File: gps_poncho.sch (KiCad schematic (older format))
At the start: 5 parts, among them J1 Micro_SD_Card, U11 SE868K3-A

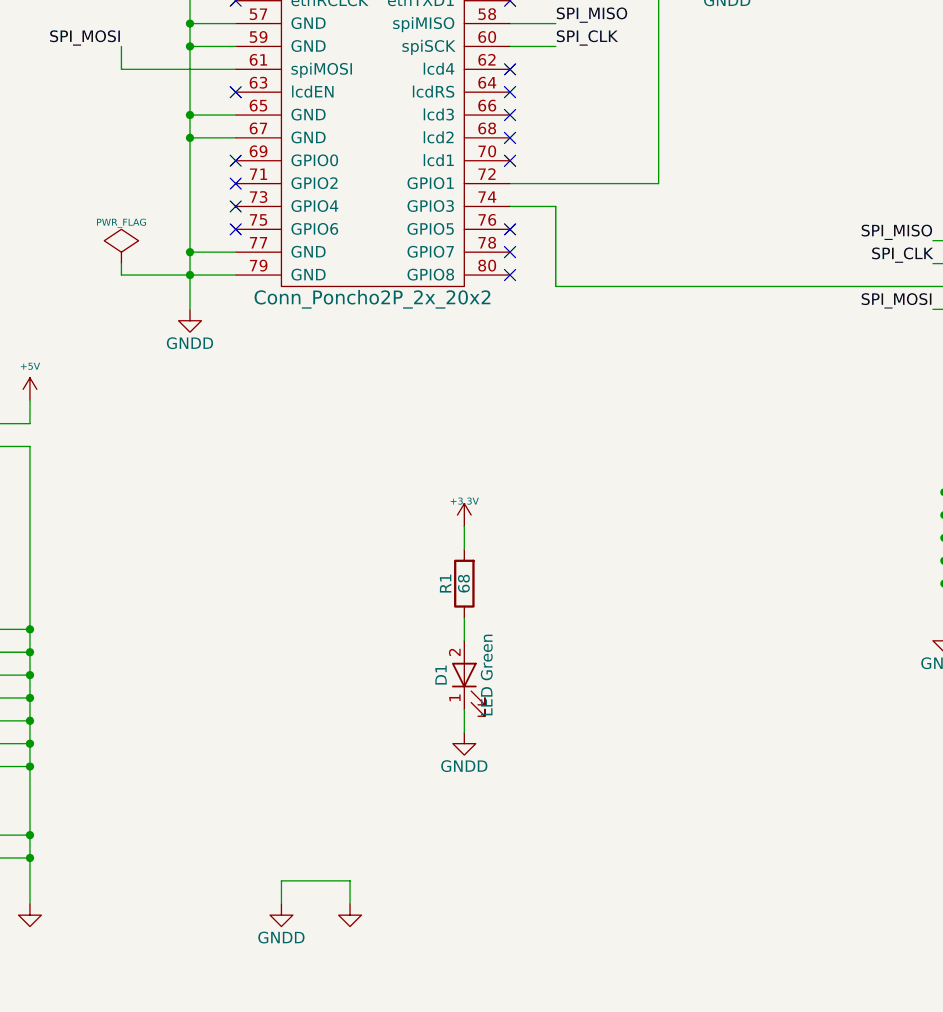
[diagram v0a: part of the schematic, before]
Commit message: Se añaden footprints y se toma en cuenta revisión de Victor Stalla. Se cambia slot de sd card
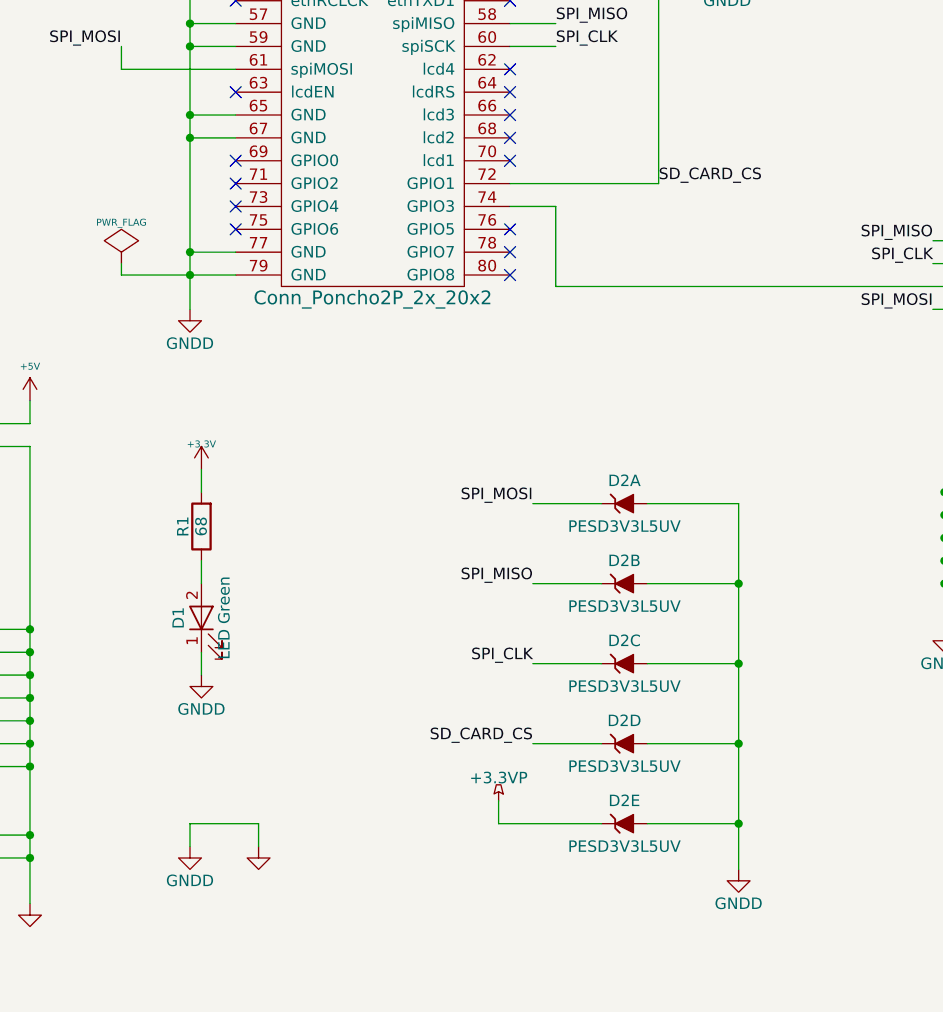
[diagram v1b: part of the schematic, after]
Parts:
- added D2: PESD3V3L5UV, footprint:SOT-666, symbol PESD3V3L5UV
- D1: footprint (none) -> footprint:LED_0805
- J1: footprint (none) -> footprint:microSD_Card_Receptacle_Wuerth_693072010801; DigiKey# WM3288TR-ND -> 732-3820-1-ND; Manf Molex, LLC -> Wurth Electronics Inc.; Manf# 0473340001 -> 693072010801
- R1: footprint (none) -> footprint:R_0805
- U11: footprint (none) -> footprint:se868A
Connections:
- net +3.3VP: now also D2.6 (K5)
- net GND: now also D2.2 (A), D2.2 (A), D2.2 (A), D2.2 (A), D2.2 (A)
- net SPI_CLK: now also D2.4 (K3)
- net SPI_MISO: now also D2.3 (K2)
- net SPI_MOSI: now also D2.1 (K1)
- net SD_CARD_CS: now reaches J1.2 (DAT3/CD), XA101.72 (GPIO1)
- net SD_CARD_CS: now also D2.5 (K4)
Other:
- moved on the sheet: D1, R1

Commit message: Primera version de PCB
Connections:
- net +3.3VP: now also R1.2
- net +3V3: no longer R1.2
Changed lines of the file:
@@
 NoConn ~ 2650 4100
-$Comp
-L +3.3V #PWR09
-U 1 1 59E3E593
-P 3600 4100
-F 0 "#PWR09" H 3600 4060 30  0001 C CNN
-F 1 "+3.3V" H 3600 4210 30  0000 C CNN
-F 2 "" H 3600 4100 60  0000 C CNN
-F 3 "" H 3600 4100 60  0000 C CNN
-	1    3600 4100
-	1    0    0    -1
-$EndComp
 $Comp
 L R R1
@@
 Wire Wire Line
 	6800 3100 7100 3100
+$Comp
+L +3.3VP #PWR?
+U 1 1 59FB3A8B
+P 3600 4100
+F 0 "#PWR?" H 3750 4050 50  0001 C CNN
+F 1 "+3.3VP" H 3600 4200 50  0000 C CNN
+F 2 "" H 3600 4100 50  0000 C CNN
+F 3 "" H 3600 4100 50  0000 C CNN
+	1    3600 4100
+	1    0    0    -1
+$EndComp
 $EndSCHEMATC
